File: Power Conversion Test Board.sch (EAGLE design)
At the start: 51 parts, among them U1 LM2678, U2 LM2678

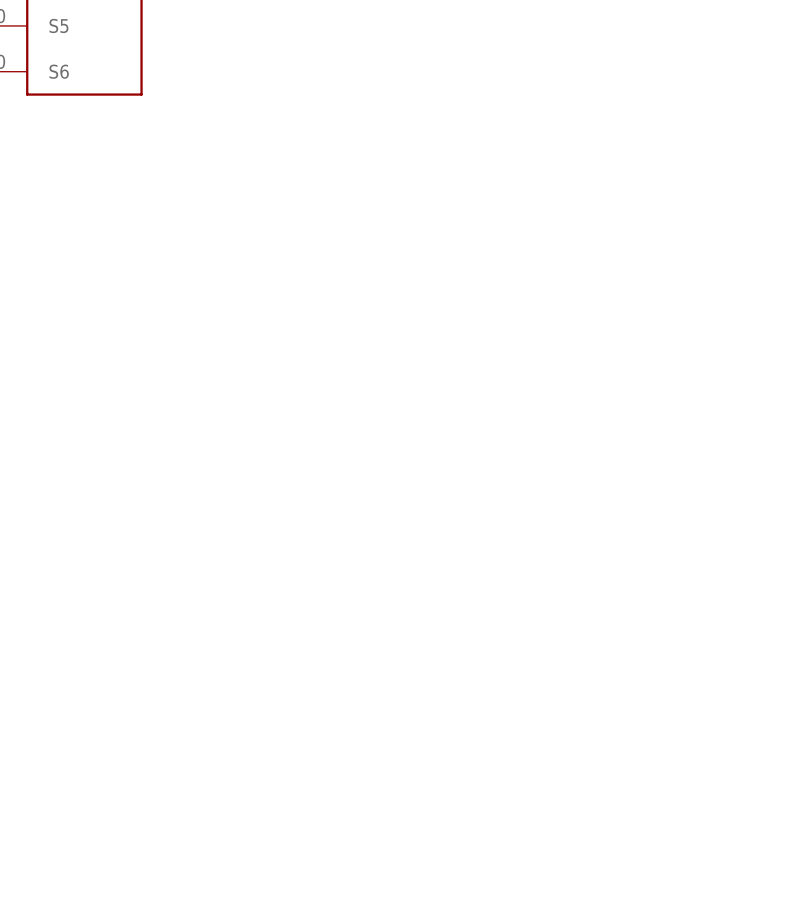
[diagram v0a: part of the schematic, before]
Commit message: added connectors
the ones that go to distribution
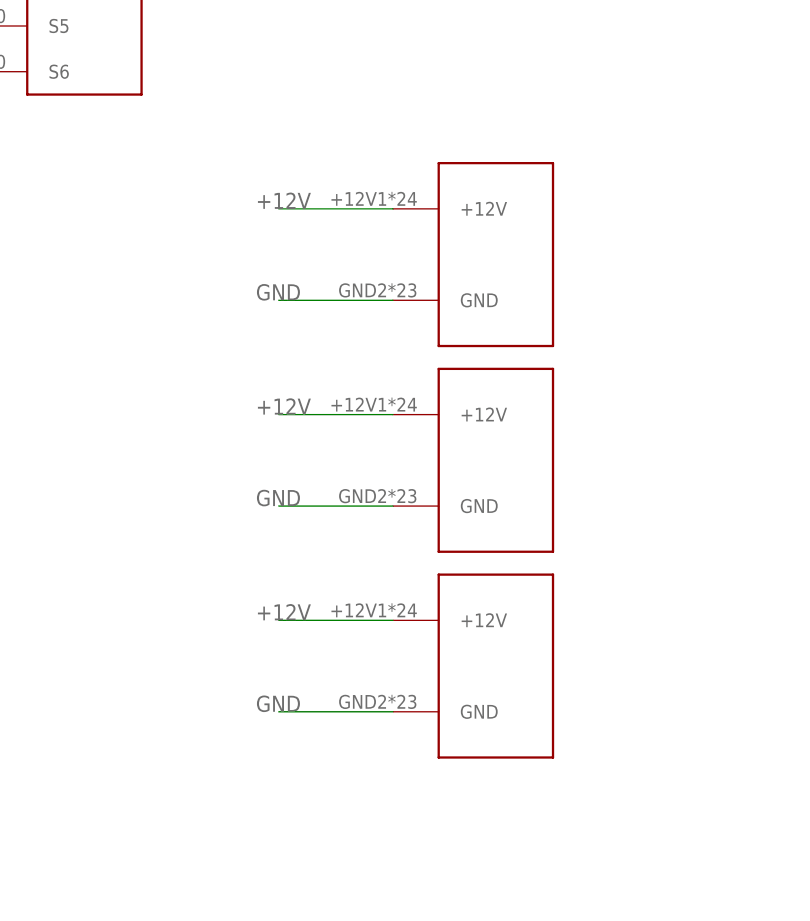
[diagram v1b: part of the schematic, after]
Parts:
- added U$12, U$13, U$14: PDB_PCB_CONNEC, PDB_PCB_connectors:PDB_PCB_CONNEC
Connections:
- new net GND: U$12.GND, U$13.GND, U$14.GND
- net +12V: now also U$12.+12V, U$13.+12V, U$14.+12V
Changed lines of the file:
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@@
 <part name="U$6" library="ET60T" deviceset="ET60T_2" device=""/>
 <part name="U$11" library="ET60T" deviceset="ET60T_2" device=""/>
+<part name="U$12" library="PDB_PCB_connectors" deviceset="PDB_PCB_CONNEC" device=""/>
+<part name="U$13" library="PDB_PCB_connectors" deviceset="PDB_PCB_CONNEC" device=""/>
+<part name="U$14" library="PDB_PCB_connectors" deviceset="PDB_PCB_CONNEC" device=""/>
 </parts>
 <sheets>
@@
 <instance part="U$11" gate="G$1" x="40.64" y="-134.62"/>
 <instance part="U$11" gate="G$2" x="99.06" y="-134.62"/>
+<instance part="U$12" gate="G$1" x="226.06" y="-93.98"/>
+<instance part="U$13" gate="G$1" x="226.06" y="-116.84"/>
+<instance part="U$14" gate="G$1" x="226.06" y="-139.7"/>
 </instances>
 <busses>
@@
 <wire x1="86.36" y1="-121.92" x2="78.74" y2="-121.92" width="0.1524" layer="91"/>
 <label x="73.66" y="-121.92" size="1.778" layer="95"/>
+</segment>
+<segment>
+<pinref part="U$12" gate="G$1" pin="+12V"/>
+<wire x1="220.98" y1="-78.74" x2="208.28" y2="-78.74" width="0.1524" layer="91"/>
+<label x="205.74" y="-78.74" size="1.778" layer="95"/>
+</segment>
+<segment>
+<pinref part="U$13" gate="G$1" pin="+12V"/>
+<wire x1="220.98" y1="-101.6" x2="208.28" y2="-101.6" width="0.1524" layer="91"/>
+<label x="205.74" y="-101.6" size="1.778" layer="95"/>
+</segment>
+<segment>
+<pinref part="U$14" gate="G$1" pin="+12V"/>
+<wire x1="220.98" y1="-124.46" x2="208.28" y2="-124.46" width="0.1524" layer="91"/>
+<label x="205.74" y="-124.46" size="1.778" layer="95"/>
 </segment>
 </net>
@@
 </segment>
 </net>
+<net name="GND" class="0">
+<segment>
+<pinref part="U$12" gate="G$1" pin="GND"/>
+<wire x1="220.98" y1="-88.9" x2="208.28" y2="-88.9" width="0.1524" layer="91"/>
+<label x="205.74" y="-88.9" size="1.778" layer="95"/>
+</segment>
+<segment>
+<pinref part="U$13" gate="G$1" pin="GND"/>
+<wire x1="220.98" y1="-111.76" x2="208.28" y2="-111.76" width="0.1524" layer="91"/>
+<label x="205.74" y="-111.76" size="1.778" layer="95"/>
+</segment>
+<segment>
+<pinref part="U$14" gate="G$1" pin="GND"/>
+<wire x1="220.98" y1="-134.62" x2="208.28" y2="-134.62" width="0.1524" layer="91"/>
+<label x="205.74" y="-134.62" size="1.778" layer="95"/>
+</segment>
+</net>

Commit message: moved board to origin
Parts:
- removed U$11, U$2, U$6: ET60T_2, ET60T:ET60T_2
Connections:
- removed net +3.3VGND: U$6G$2.S5
- net +12V: no longer U$11G$2.S1, U$2G$2.S1, U$6G$2.S1
- net +3.3V: no longer U$11G$2.S5, U$2G$2.S5
- net +5V: no longer U$11G$2.S3, U$2G$2.S3, U$6G$2.S3
- net 12VGND: no longer U$11G$2.S2, U$2G$2.S2, U$6G$2.S2
- net 3.3VGND: no longer U$11G$2.S6, U$2G$2.S6, U$6G$2.S6
- net 5VGND: no longer U$11G$2.S4, U$2G$2.S4, U$6G$2.S4

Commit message: Did stuff and corrected stuff
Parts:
- added U$11, U$2, U$6: ET60S, ET60S:ET60S
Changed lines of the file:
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@@
 <?xml version="1.0" encoding="utf-8"?>
 <!DOCTYPE eagle SYSTEM "eagle.dtd">
-<eagle version="9.2.0">
+<eagle version="9.1.3">
 <drawing>
 <settings>
@@
 <part name="U$13" library="PDB_PCB_connectors" deviceset="PDB_PCB_CONNEC" device=""/>
 <part name="U$14" library="PDB_PCB_connectors" deviceset="PDB_PCB_CONNEC" device=""/>
+<part name="U$2" library="ET60S" deviceset="ET60S" device=""/>
+<part name="U$6" library="ET60S" deviceset="ET60S" device=""/>
+<part name="U$11" library="ET60S" deviceset="ET60S" device=""/>
 </parts>
 <sheets>
@@
 <instance part="U$13" gate="G$1" x="226.06" y="-116.84"/>
 <instance part="U$14" gate="G$1" x="226.06" y="-139.7"/>
+<instance part="U$2" gate="G$1" x="27.94" y="-27.94"/>
+<instance part="U$2" gate="G$2" x="27.94" y="-86.36"/>
+<instance part="U$6" gate="G$1" x="68.58" y="-27.94"/>
+<instance part="U$6" gate="G$2" x="68.58" y="-86.36"/>
+<instance part="U$11" gate="G$1" x="106.68" y="-27.94"/>
+<instance part="U$11" gate="G$2" x="106.68" y="-86.36"/>
 </instances>
 <busses>

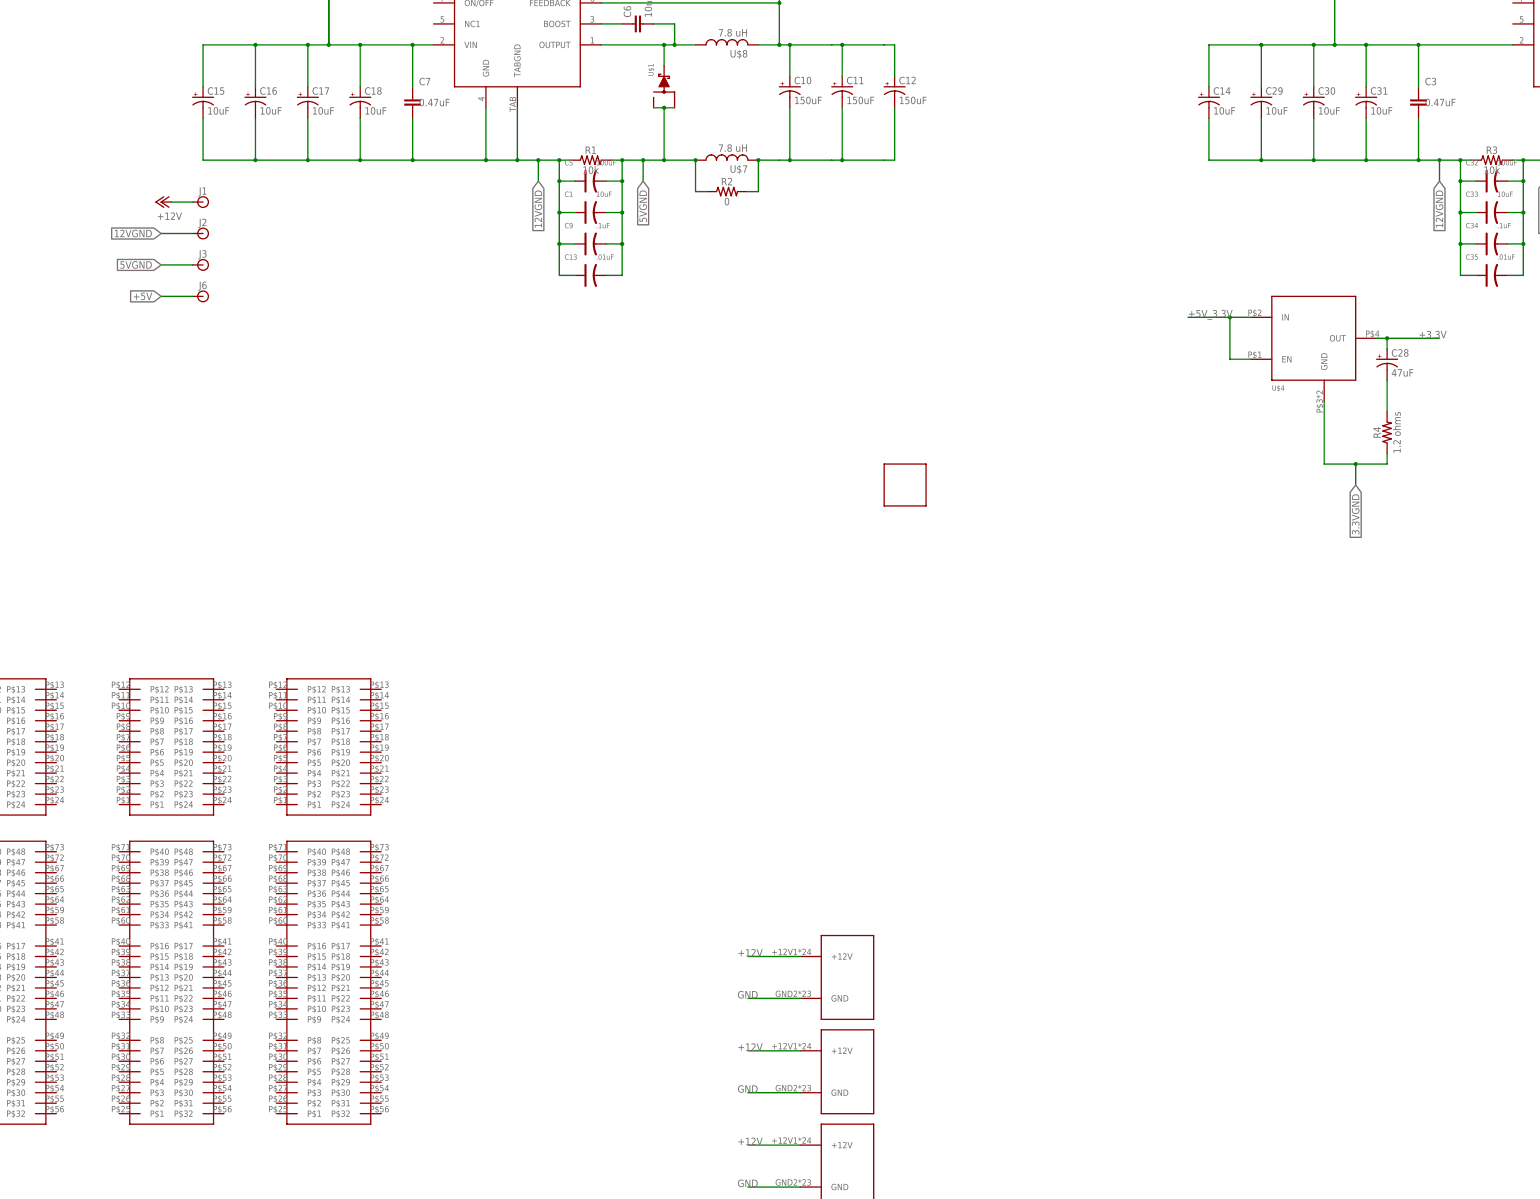
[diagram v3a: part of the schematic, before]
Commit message: Added the updated ET60S connectors
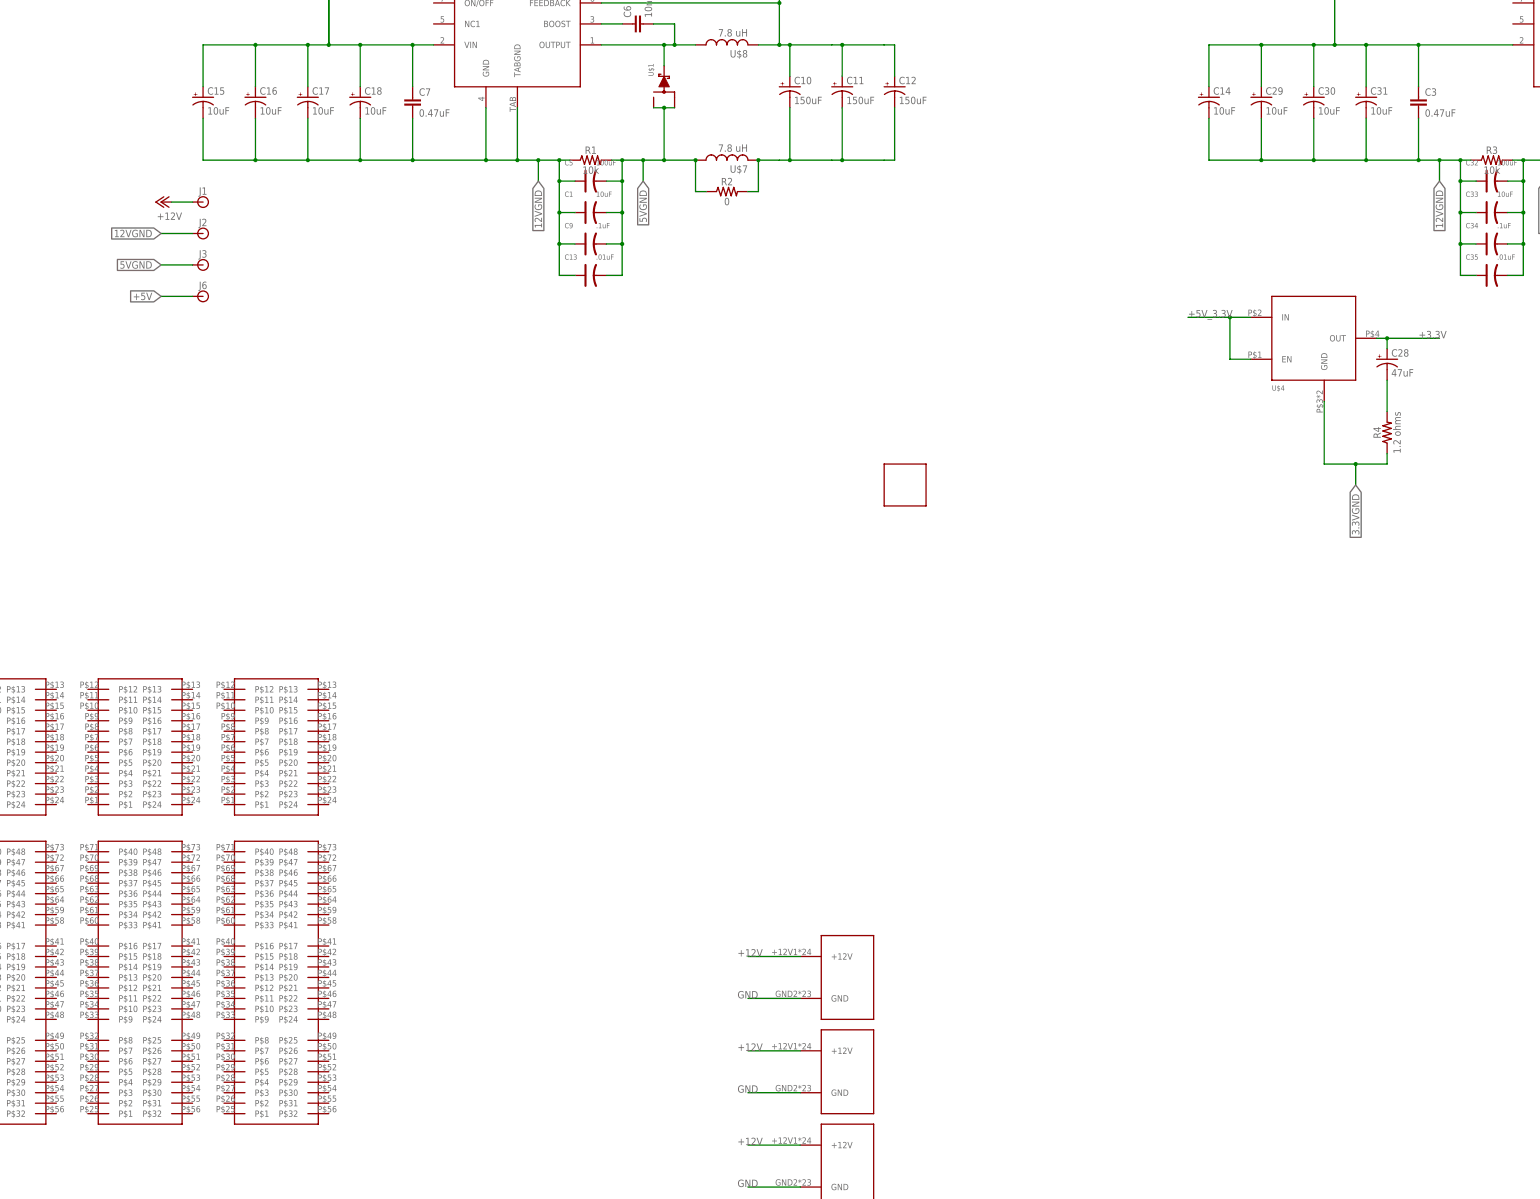
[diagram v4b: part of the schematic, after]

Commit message: Changed stuff
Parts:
- removed U$11, U$2, U$6: ET60S, ET60S:ET60S
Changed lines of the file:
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@@
 <?xml version="1.0" encoding="utf-8"?>
 <!DOCTYPE eagle SYSTEM "eagle.dtd">
-<eagle version="9.2.2">
+<eagle version="9.1.3">
 <drawing>
 <settings>
@@
 <part name="U$13" library="PDB_PCB_connectors" deviceset="PDB_PCB_CONNEC" device=""/>
 <part name="U$14" library="PDB_PCB_connectors" deviceset="PDB_PCB_CONNEC" device=""/>
-<part name="U$2" library="ET60S" deviceset="ET60S" device=""/>
-<part name="U$6" library="ET60S" deviceset="ET60S" device=""/>
-<part name="U$11" library="ET60S" deviceset="ET60S" device=""/>
 </parts>
 <sheets>
@@
 <instance part="U$13" gate="G$1" x="226.06" y="-116.84" smashed="yes"/>
 <instance part="U$14" gate="G$1" x="226.06" y="-139.7" smashed="yes"/>
-<instance part="U$2" gate="G$1" x="27.94" y="-27.94" smashed="yes"/>
-<instance part="U$2" gate="G$2" x="27.94" y="-86.36" smashed="yes"/>
-<instance part="U$6" gate="G$1" x="60.96" y="-27.94" smashed="yes"/>
-<instance part="U$6" gate="G$2" x="60.96" y="-86.36" smashed="yes"/>
-<instance part="U$11" gate="G$1" x="93.98" y="-27.94" smashed="yes"/>
-<instance part="U$11" gate="G$2" x="93.98" y="-86.36" smashed="yes"/>
 </instances>
 <busses>

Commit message: Made some minor changes to the board, just uploading for saving purposes
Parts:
- removed R2, R5: 0, SparkFun-Resistors:RESISTOR0603
- removed U$12, U$13, U$14: PDB_PCB_CONNEC, PDB_PCB_connectors:PDB_PCB_CONNEC
- added R6, R7: 0, audio amplifier example:R-US_R1206
- added U$2: PDB_PCB_CONNEC, PDB_PCB_connectors:PDB_PCB_CONNEC
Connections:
- net +12V: now also U$2.+12V; no longer U$12.+12V, U$13.+12V, U$14.+12V
- net 3.3VGND: now also R6.1; no longer R5.1
- net 5VGND: now also R7.1; no longer R2.1
- net GND: now also U$2.GND; no longer U$12.GND, U$13.GND, U$14.GND
- net N$4: now also R6.2; no longer R5.2
- net N$8: now also R7.2; no longer R2.2
